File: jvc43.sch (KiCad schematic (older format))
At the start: 0 parts

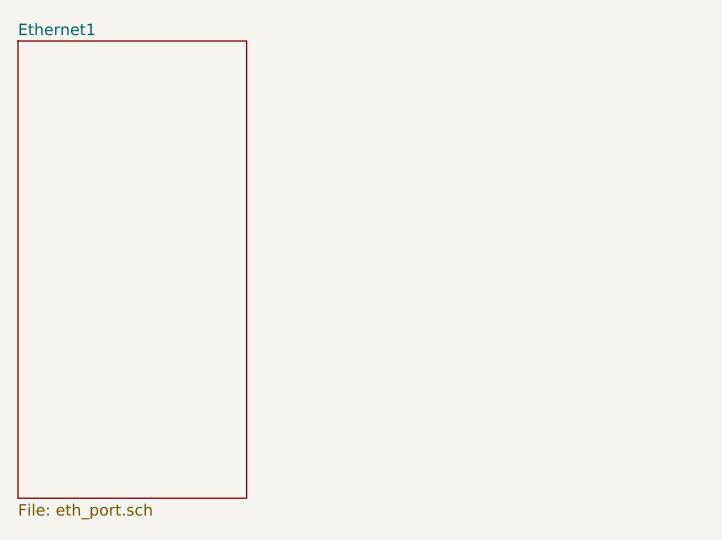
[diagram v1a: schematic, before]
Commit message: - Selected a shielded RJ45 with dual LEDs, with the cable orientation such   that it makes the transformer-to-RJ45 wiring nice. - Added a second whole Ethernet port and connected the two ports together at   the top level.
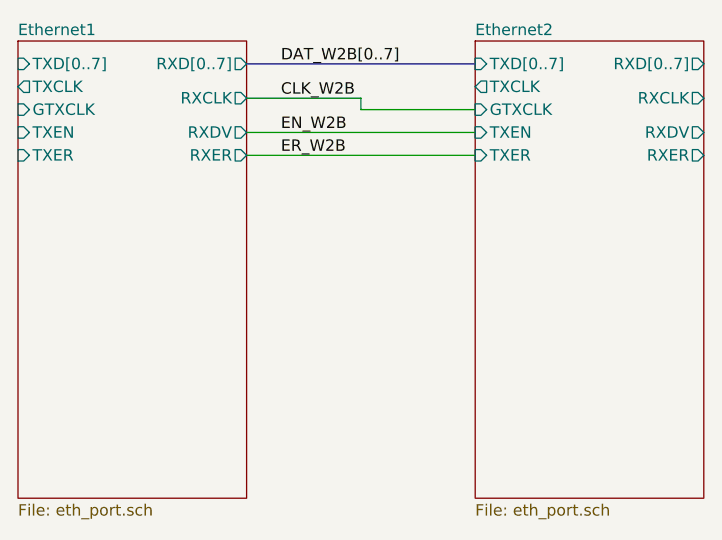
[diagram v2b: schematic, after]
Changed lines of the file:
@@
 $Descr B 17000 11000
 encoding utf-8
-Sheet 1 2
+Sheet 1 3
 Title "JVC43A"
 Date "2022-12-05"
@@
 F0 "Ethernet1" 50
 F1 "eth_port.sch" 50
+F2 "RXD[0..7]" O R 3000 1100 50
+F3 "TXD[0..7]" I L 2000 1100 50
+F4 "RXCLK" O R 3000 1250 50
+F5 "RXDV" O R 3000 1400 50
+F6 "RXER" O R 3000 1500 50
+F7 "TXCLK" O L 2000 1200 50
+F8 "GTXCLK" I L 2000 1300 50
+F9 "TXEN" I L 2000 1400 50
+F10 "TXER" I L 2000 1500 50
 $EndSheet
+$Sheet
+S 4000 1000 1000 2000
+U 638EC3A5
+F0 "Ethernet2" 50
+F1 "eth_port.sch" 50
+F2 "RXD[0..7]" O R 5000 1100 50
+F3 "TXD[0..7]" I L 4000 1100 50
+F4 "RXCLK" O R 5000 1250 50
+F5 "RXDV" O R 5000 1400 50
+F6 "RXER" O R 5000 1500 50
+F7 "TXCLK" O L 4000 1200 50
+F8 "GTXCLK" I L 4000 1300 50
+F9 "TXEN" I L 4000 1400 50
+F10 "TXER" I L 4000 1500 50
+$EndSheet
+Wire Bus Line
+	3000 1100 4000 1100
+Wire Wire Line
+	3000 1250 3500 1250
+Wire Wire Line
+	3500 1250 3500 1300
+Wire Wire Line
+	3500 1300 4000 1300
+Wire Wire Line
+	3000 1400 4000 1400
+Wire Wire Line
+	3000 1500 4000 1500
+Text Label 3150 1100 0    50   ~ 0
+DAT_W2B[0..7]
+Text Label 3150 1250 0    50   ~ 0
+CLK_W2B
+Text Label 3150 1400 0    50   ~ 0
+EN_W2B
+Text Label 3150 1500 0    50   ~ 0
+ER_W2B
 $EndSCHEMATC

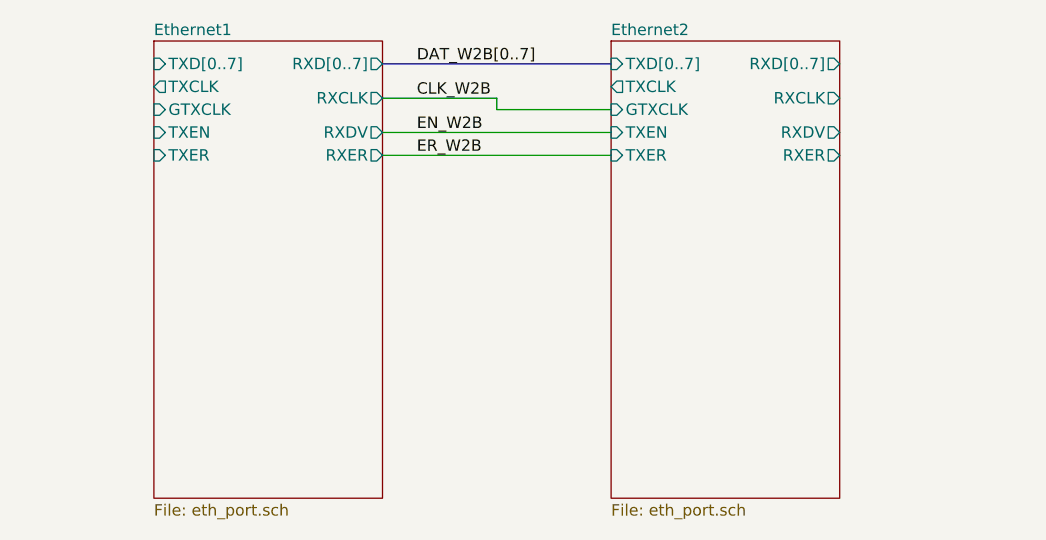
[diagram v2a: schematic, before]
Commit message: Lots of work. - Bussed the two Ethernet blocks together in top level schematic - Mashed Ethernet1 input wires to ground - Added hierarchical label for crystal-in pin - Added a couple more net labels for clarity when routing - Routed Ethernet1 transformer-to-PHY area *including* most of those passives! - Selected a new board shape and started mashing things to fit
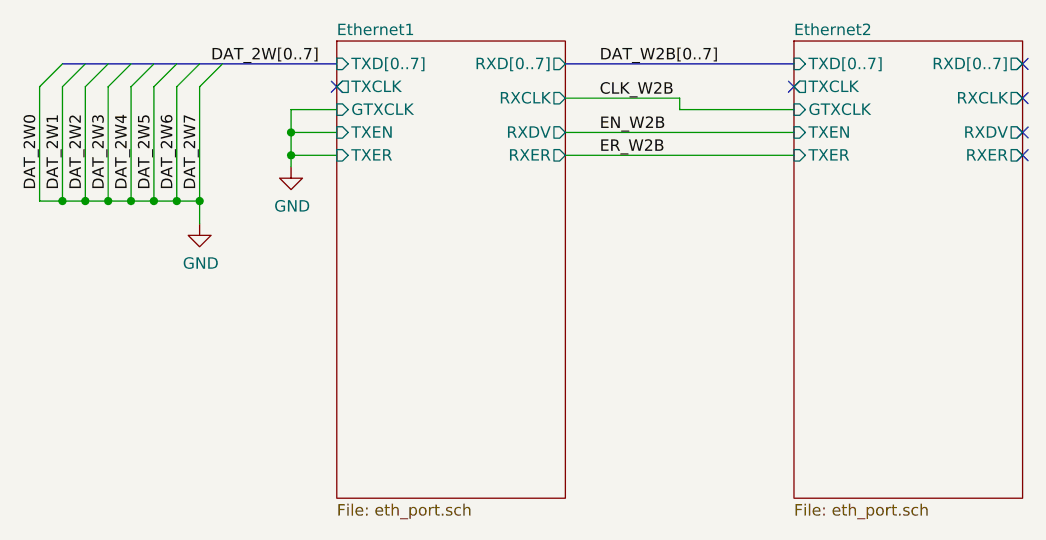
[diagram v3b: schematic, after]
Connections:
- no-connect marks 0 -> 6
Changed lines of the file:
@@
 $EndDescr
 $Sheet
-S 2000 1000 1000 2000
+S 2800 1000 1000 2000
 U 638E68FB
 F0 "Ethernet1" 50
 F1 "eth_port.sch" 50
-F2 "RXD[0..7]" O R 3000 1100 50
-F3 "TXD[0..7]" I L 2000 1100 50
-F4 "RXCLK" O R 3000 1250 50
-F5 "RXDV" O R 3000 1400 50
-F6 "RXER" O R 3000 1500 50
-F7 "TXCLK" O L 2000 1200 50
-F8 "GTXCLK" I L 2000 1300 50
-F9 "TXEN" I L 2000 1400 50
-F10 "TXER" I L 2000 1500 50
+F2 "RXD[0..7]" O R 3800 1100 50
+F3 "TXD[0..7]" I L 2800 1100 50
+F4 "RXCLK" O R 3800 1250 50
+F5 "RXDV" O R 3800 1400 50
+F6 "RXER" O R 3800 1500 50
+F7 "TXCLK" O L 2800 1200 50
+F8 "GTXCLK" I L 2800 1300 50
+F9 "TXEN" I L 2800 1400 50
+F10 "TXER" I L 2800 1500 50
 $EndSheet
 $Sheet
-S 4000 1000 1000 2000
+S 4800 1000 1000 2000
 U 638EC3A5
 F0 "Ethernet2" 50
 F1 "eth_port.sch" 50
-F2 "RXD[0..7]" O R 5000 1100 50
-F3 "TXD[0..7]" I L 4000 1100 50
-F4 "RXCLK" O R 5000 1250 50
-F5 "RXDV" O R 5000 1400 50
-F6 "RXER" O R 5000 1500 50
-F7 "TXCLK" O L 4000 1200 50
-F8 "GTXCLK" I L 4000 1300 50
-F9 "TXEN" I L 4000 1400 50
-F10 "TXER" I L 4000 1500 50
+F2 "RXD[0..7]" O R 5800 1100 50
+F3 "TXD[0..7]" I L 4800 1100 50
+F4 "RXCLK" O R 5800 1250 50
+F5 "RXDV" O R 5800 1400 50
+F6 "RXER" O R 5800 1500 50
+F7 "TXCLK" O L 4800 1200 50
+F8 "GTXCLK" I L 4800 1300 50
+F9 "TXEN" I L 4800 1400 50
+F10 "TXER" I L 4800 1500 50
 $EndSheet
 Wire Bus Line
-	3000 1100 4000 1100
+	3800 1100 4800 1100
 Wire Wire Line
-	3000 1250 3500 1250
+	3800 1250 4300 1250
 Wire Wire Line
-	3500 1250 3500 1300
+	4300 1250 4300 1300
 Wire Wire Line
-	3500 1300 4000 1300
+	4300 1300 4800 1300
 Wire Wire Line
-	3000 1400 4000 1400
+	3800 1400 4800 1400
 Wire Wire Line
-	3000 1500 4000 1500
-Text Label 3150 1100 0    50   ~ 0
+	3800 1500 4800 1500
+Text Label 3950 1100 0    50   ~ 0
 DAT_W2B[0..7]
-Text Label 3150 1250 0    50   ~ 0
+Text Label 3950 1250 0    50   ~ 0
 CLK_W2B
-Text Label 3150 1400 0    50   ~ 0
+Text Label 3950 1400 0    50   ~ 0
 EN_W2B
-Text Label 3150 1500 0    50   ~ 0
+Text Label 3950 1500 0    50   ~ 0
 ER_W2B
+Wire Wire Line
+	2800 1300 2600 1300
+Wire Wire Line
+	2600 1300 2600 1400
+$Comp
+L power:GND #PWR0101
+U 1 1 639093A1
+P 2600 1550
+F 0 "#PWR0101" H 2600 1300 50  0001 C CNN
+F 1 "GND" H 2605 1377 50  0000 C CNN
+F 2 "" H 2600 1550 50  0001 C CNN
+F 3 "" H 2600 1550 50  0001 C CNN
+	1    2600 1550
+	1    0    0    -1
+$EndComp
+Wire Wire Line
+	2800 1500 2600 1500
+Connection ~ 2600 1500
+Wire Wire Line
+	2600 1500 2600 1550
+Wire Wire Line
+	2800 1400 2600 1400
+Connection ~ 2600 1400
+Wire Wire Line
+	2600 1400 2600 1500
+Text Label 2250 1100 0    50   ~ 0
+DAT_2W[0..7]
+Entry Wire Line
+	1700 1200 1800 1100
+Entry Wire Line
+	1800 1200 1900 1100
+Entry Wire Line
+	1500 1200 1600 1100
+Entry Wire Line
+	1600 1200 1700 1100
+Entry Wire Line
+	2100 1200 2200 1100
+Entry Wire Line
+	2200 1200 2300 1100
+Entry Wire Line
+	1900 1200 2000 1100
+Entry Wire Line
+	2000 1200 2100 1100
+Wire Wire Line
+	1500 1200 1500 1700
+Text Label 1500 1650 1    50   ~ 0
+DAT_2W0
+Wire Wire Line
+	1600 1200 1600 1700
+Text Label 1600 1650 1    50   ~ 0
+DAT_2W1
+Wire Wire Line
+	1700 1200 1700 1700
+Text Label 1700 1650 1    50   ~ 0
+DAT_2W2
+Wire Wire Line
+	1800 1200 1800 1700
+Text Label 1800 1650 1    50   ~ 0
+DAT_2W3
+Wire Wire Line
+	1900 1200 1900 1700
+Text Label 1900 1650 1    50   ~ 0
+DAT_2W4
+Wire Wire Line
+	2000 1200 2000 1700
+Text Label 2000 1650 1    50   ~ 0
+DAT_2W5
+Wire Wire Line
+	2100 1200 2100 1700
+Text Label 2100 1650 1    50   ~ 0
+DAT_2W6
+Wire Wire Line
+	2200 1200 2200 1700
+Text Label 2200 1650 1    50   ~ 0
+DAT_2W7
+Wire Wire Line
+	1500 1700 1600 1700
+Connection ~ 1600 1700
+Wire Wire Line
+	1600 1700 1700 1700
+Connection ~ 1700 1700
+Wire Wire Line
+	1700 1700 1800 1700
+Connection ~ 1800 1700
+Wire Wire Line
+	1800 1700 1900 1700
+Connection ~ 1900 1700
+Wire Wire Line
+	1900 1700 2000 1700
+Connection ~ 2000 1700
+Wire Wire Line
+	2000 1700 2100 1700
+Connection ~ 2100 1700
+Wire Wire Line
+	2100 1700 2200 1700
+Wire Wire Line
+	2200 1800 2200 1700
+Connection ~ 2200 1700
+$Comp
+L power:GND #PWR0102
+U 1 1 6390ACF0
+P 2200 1800
+F 0 "#PWR0102" H 2200 1550 50  0001 C CNN
+F 1 "GND" H 2205 1627 50  0000 C CNN
+F 2 "" H 2200 1800 50  0001 C CNN
+F 3 "" H 2200 1800 50  0001 C CNN
+	1    2200 1800
+	1    0    0    -1
+$EndComp
+NoConn ~ 2800 1200
+NoConn ~ 4800 1200
+NoConn ~ 5800 1100
+NoConn ~ 5800 1250
+NoConn ~ 5800 1400
+NoConn ~ 5800 1500
+Wire Bus Line
+	1600 1100 2800 1100
 $EndSCHEMATC

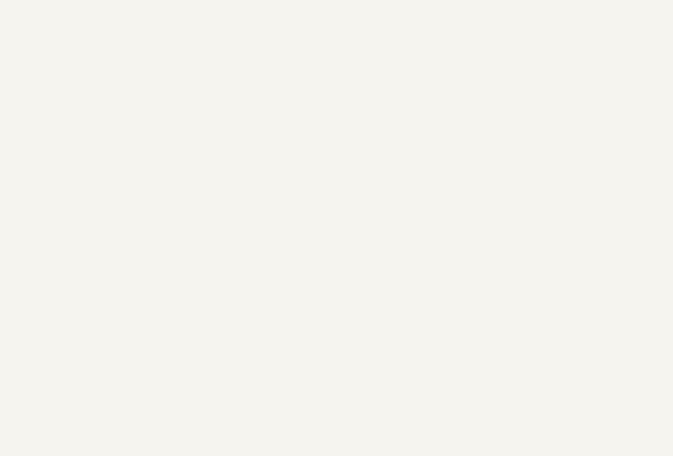
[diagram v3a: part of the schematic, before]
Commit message: - Added copyright and license headers to the schematic - Started in on the power supply, from 0 to 80% or so, including documentation
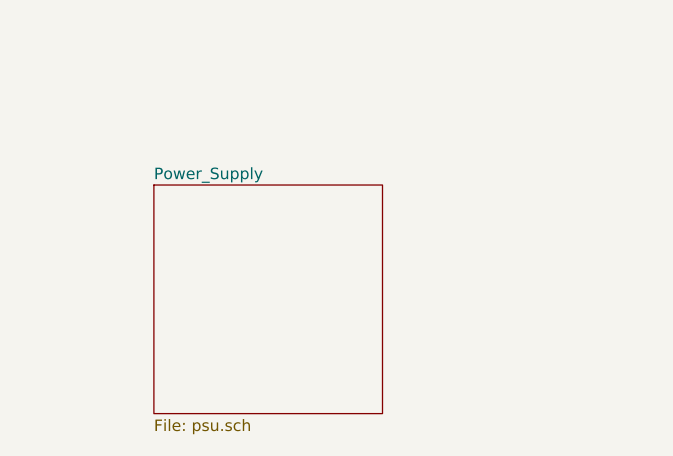
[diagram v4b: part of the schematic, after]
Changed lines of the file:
@@
 $Descr B 17000 11000
 encoding utf-8
-Sheet 1 3
+Sheet 1 4
 Title "JVC43A"
-Date "2022-12-05"
-Rev "NC"
-Comp ""
-Comment1 ""
+Date "2022-12-07"
+Rev "1"
+Comp "©2022 OT Collective"
+Comment1 "Licensed under the TAPR Open Hardware License v1.0"
 Comment2 ""
 Comment3 ""
@@
 NoConn ~ 5800 1400
 NoConn ~ 5800 1500
+$Sheet
+S 2000 4000 1000 1000
+U 63912954
+F0 "Power_Supply" 50
+F1 "psu.sch" 50
+$EndSheet
 Wire Bus Line
 	1600 1100 2800 1100

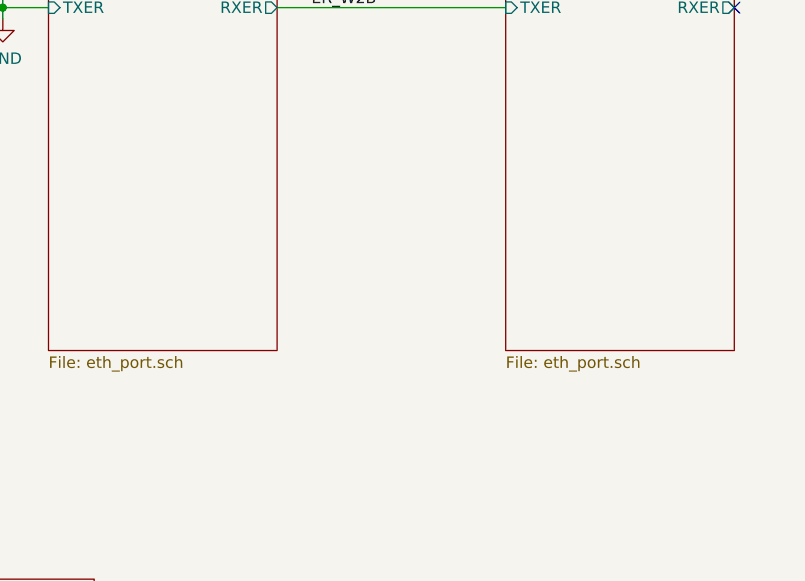
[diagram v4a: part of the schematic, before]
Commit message: Forward progress - Started the real 1.2V power plane - Placed and routed most of PHY1 decoupling capacitors - Placed and partly routed transformer2 PHY-side resistors & capacitors - Labelled a few more nets for clarity during layout
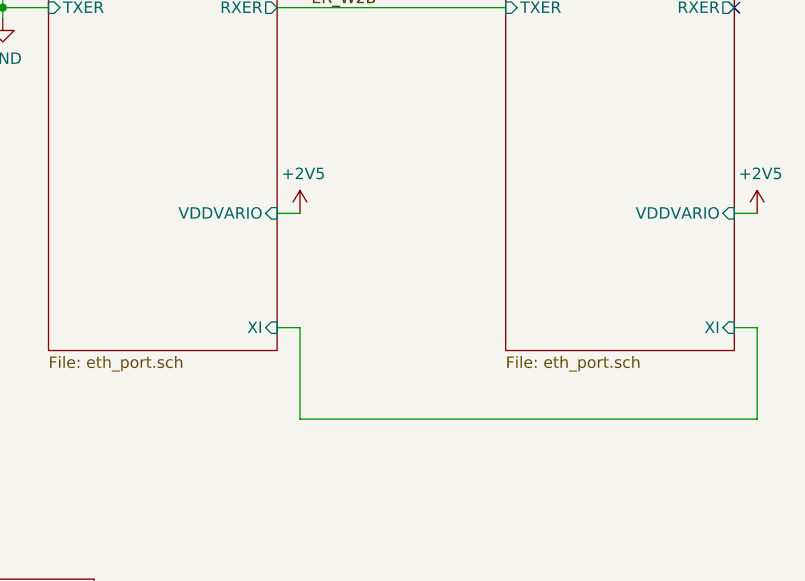
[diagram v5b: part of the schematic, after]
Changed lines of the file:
@@
 F9 "TXEN" I L 2800 1400 50
 F10 "TXER" I L 2800 1500 50
+F11 "VDDVARIO" I R 3800 2400 50
+F12 "XI" I R 3800 2900 50
 $EndSheet
 $Sheet
@@
 F9 "TXEN" I L 4800 1400 50
 F10 "TXER" I L 4800 1500 50
+F11 "VDDVARIO" I R 5800 2400 50
+F12 "XI" I R 5800 2900 50
 $EndSheet
 Wire Bus Line
@@
 F1 "psu.sch" 50
 $EndSheet
+Wire Wire Line
+	3800 2400 3900 2400
+$Comp
+L power:+2V5 #PWR?
+U 1 1 63A0D2C7
+P 3900 2400
+F 0 "#PWR?" H 3900 2250 50  0001 C CNN
+F 1 "+2V5" H 3915 2573 50  0000 C CNN
+F 2 "" H 3900 2400 50  0001 C CNN
+F 3 "" H 3900 2400 50  0001 C CNN
+	1    3900 2400
+	1    0    0    -1
+$EndComp
+Wire Wire Line
+	5800 2400 5900 2400
+$Comp
+L power:+2V5 #PWR?
+U 1 1 63A0D2DA
+P 5900 2400
+F 0 "#PWR?" H 5900 2250 50  0001 C CNN
+F 1 "+2V5" H 5915 2573 50  0000 C CNN
+F 2 "" H 5900 2400 50  0001 C CNN
+F 3 "" H 5900 2400 50  0001 C CNN
+	1    5900 2400
+	1    0    0    -1
+$EndComp
+Wire Wire Line
+	3800 2900 3900 2900
+Wire Wire Line
+	3900 2900 3900 3300
+Wire Wire Line
+	3900 3300 5900 3300
+Wire Wire Line
+	5900 3300 5900 2900
+Wire Wire Line
+	5900 2900 5800 2900
 Wire Bus Line
 	1600 1100 2800 1100
